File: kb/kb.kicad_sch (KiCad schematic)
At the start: 90 parts, among them SW1 SW_Push, SW10 SW_Push, SW11 SW_Push, SW12 SW_Push, SW13 SW_Push, SW14 SW_Push, SW15 SW_Push, SW16 SW_Push, SW17 SW_Push, SW18 SW_Push, SW19 SW_Push, SW2 SW_Push, SW20 SW_Push, SW21 SW_Push, SW22 SW_Push, SW23 SW_Push, SW24 SW_Push, SW25 SW_Push, SW26 SW_Push, SW27 SW_Push, SW28 SW_Push, SW29 SW_Push, SW3 SW_Push, SW30 SW_Push, SW31 SW_Push, SW32 SW_Push, SW33 SW_Push, SW34 SW_Push, SW35 SW_Push, SW36 SW_Push, SW37 SW_Push, SW38 SW_Push, SW39 SW_Push, SW4 SW_Push, SW40 SW_Push, SW41 SW_Push, SW42 SW_Push, SW43 SW_Push, SW44 SW_Push, SW45 SW_Push, SW5 SW_Push, SW6 SW_Push, SW7 SW_Push, SW8 SW_Push, SW9 SW_Push

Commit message: Updated Schematic
Updated Schematic
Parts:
- added D46: D, Diode_SMD:D_0201_0603Metric, symbol Device:D
- added SW24: SW_Push, MX_Solderable:MX-Solderable-1.5U, symbol Switch:SW_Push
- SW1: footprint MX_Solderable:MX-Solderable-1U -> MX_Solderable:MX-Solderable-1.5U
- SW12, SW13: footprint MX_Solderable:MX-Solderable-1U -> MX_Solderable:MX-Solderable-1.75U
- SW25: renamed from SW24; footprint MX_Solderable:MX-Solderable-1U -> MX_Solderable:MX-Solderable-2.25U
- SW37: renamed from SW36; footprint MX_Solderable:MX-Solderable-1U -> MX_Solderable:MX-Solderable-1.25U
- SW39: renamed from SW38; footprint MX_Solderable:MX-Solderable-1U -> MX_Solderable:MX-Solderable-1.25U
- SW40: renamed from SW39; footprint MX_Solderable:MX-Solderable-1U -> MX_Solderable:MX-Solderable-2.25U
- SW42: renamed from SW41; footprint MX_Solderable:MX-Solderable-1U -> MX_Solderable:MX-Solderable-2.25U
- SW43: renamed from SW42; footprint MX_Solderable:MX-Solderable-1U -> MX_Solderable:MX-Solderable-1.25U
- renumbered SW25 to SW26, SW26 to SW27, SW27 to SW28, SW28 to SW29, SW29 to SW30, SW30 to SW31, SW31 to SW32, SW32 to SW33, SW33 to SW34, SW34 to SW35, SW35 to SW36, SW37 to SW38, SW40 to SW41, SW43 to SW44, SW44 to SW45, SW45 to SW46
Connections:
- net COL11: now also SW24.1
- net ROW1: now also D46.1 (K)
- new net: D46.2 (A), SW24.2

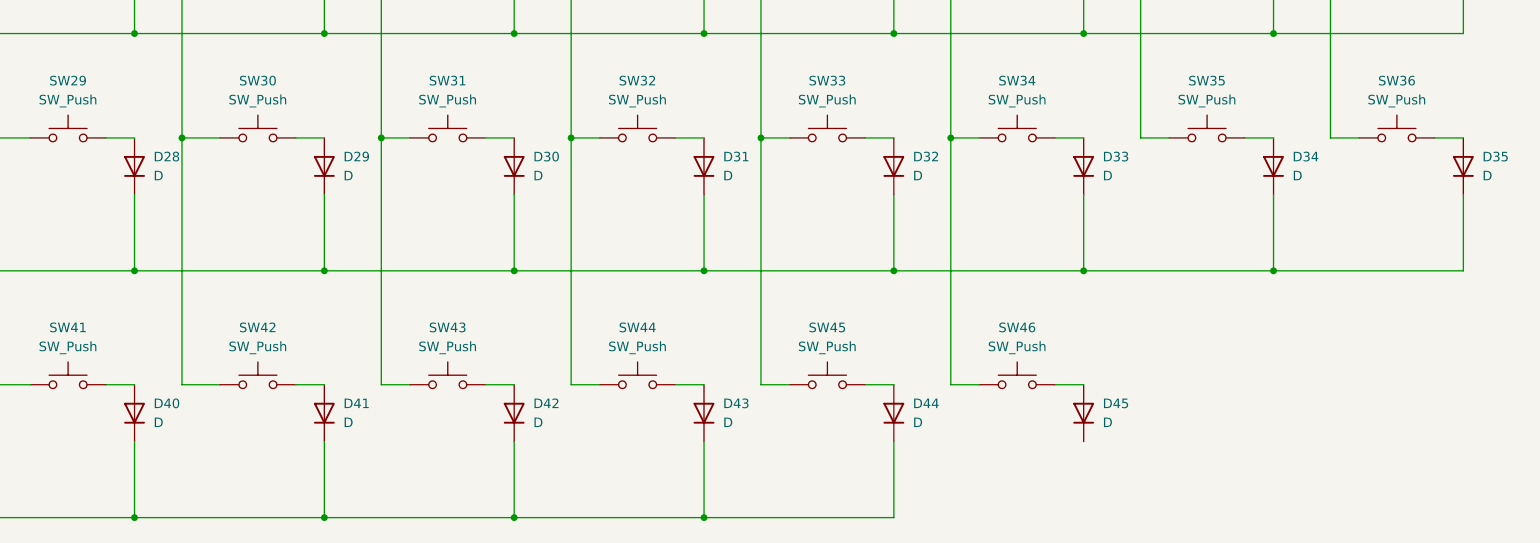
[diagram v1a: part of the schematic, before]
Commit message: Improved routing
Edited schematic column layout,
Manually routed necessary keys on pcb
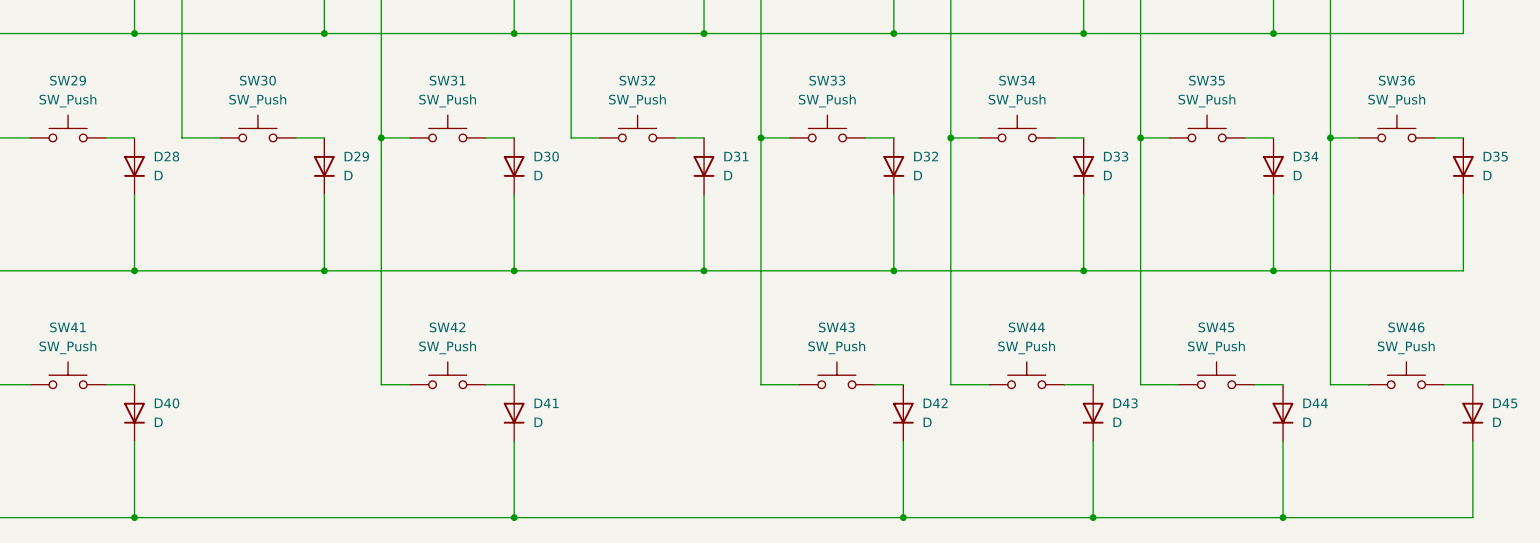
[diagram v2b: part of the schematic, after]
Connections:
- net COL10: now also SW45.1
- net COL11: now also SW46.1
- net COL5: no longer SW42.1
- net COL6: now also SW42.1; no longer SW43.1
- net COL7: no longer SW44.1
- net COL8: now also SW43.1; no longer SW45.1
- net COL9: now also SW44.1; no longer SW46.1
- net ROW3: now also D45.1 (K)
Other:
- moved on the sheet: D41, D42, D43, D44, D45, SW42, SW43, SW44, SW45, SW46

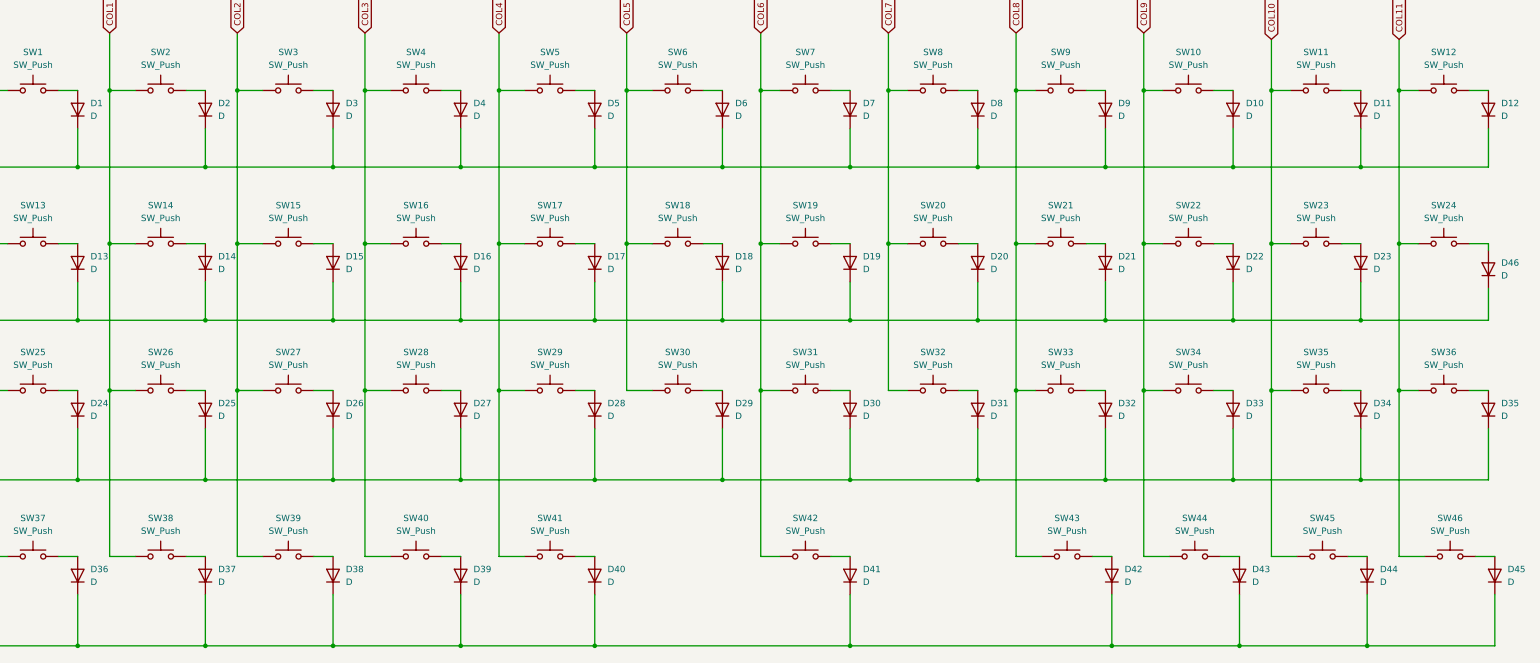
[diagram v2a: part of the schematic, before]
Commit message: 1.5u enter, fixed schematic
Fixed schematic & pcb for 1.5u enter layout
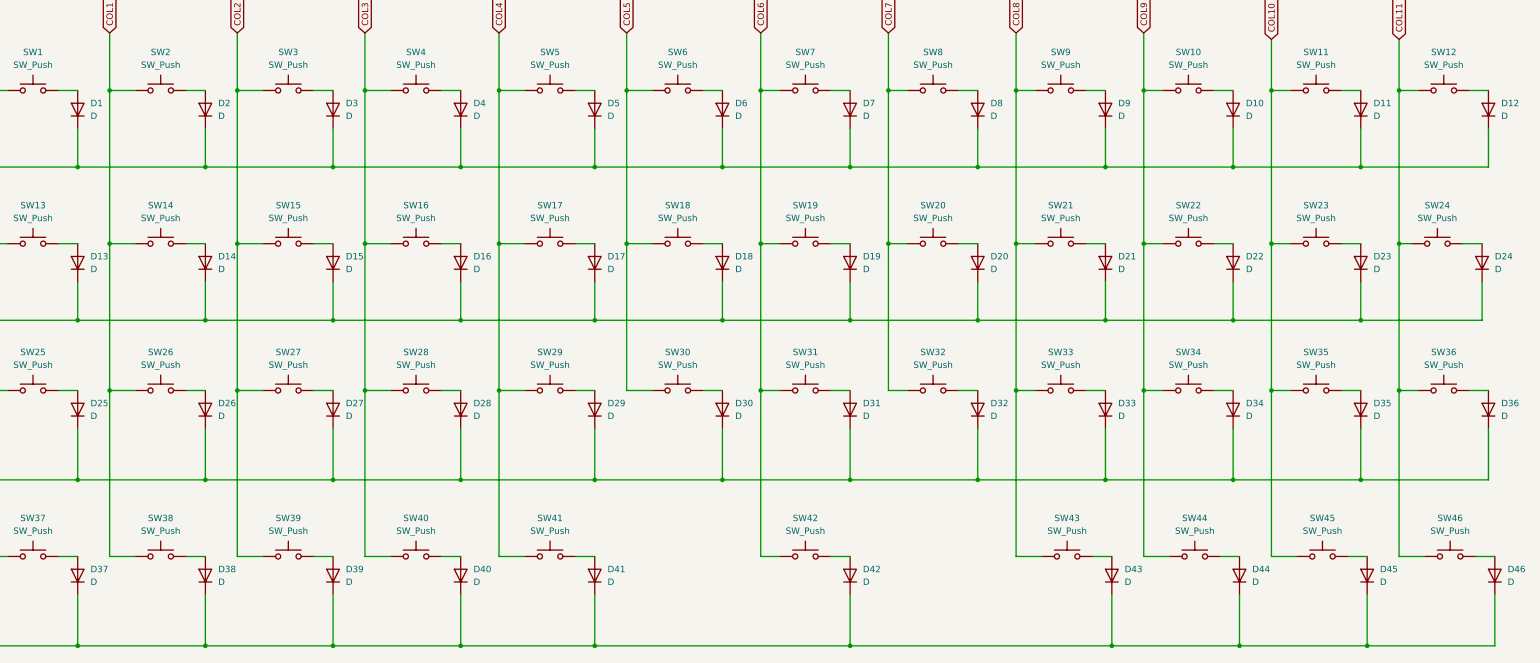
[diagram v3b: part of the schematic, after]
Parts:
- removed D46: D, Diode_SMD:D_0201_0603Metric, symbol Device:D
- added D24: D, Diode_SMD:D_0201_0603Metric, symbol Device:D
- renumbered D24 to D25, D25 to D26, D26 to D27, D27 to D28, D28 to D29, D29 to D30, D30 to D31, D31 to D32, D32 to D33, D33 to D34, D34 to D35, D35 to D36, D36 to D37, D37 to D38, D38 to D39, D39 to D40, D40 to D41, D41 to D42, D42 to D43, D43 to D44, D44 to D45, D45 to D46
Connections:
- net ROW1: now also D24.1 (K)
- net at SW24.2: now also D24.2 (A)

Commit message: STM32 + Unified Daughterboard Implementation
Switched to run off STM32 and S1.1 Unified Daughterboard.
Wired rows and cols
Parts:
- added C10, C12, C9: 1uF, Capacitor_SMD:C_0805_2012Metric, symbol Device:C_Small
- added C11: 10nF, Capacitor_SMD:C_0805_2012Metric, symbol Device:C_Small
- added C13, C8: 100nF, Capacitor_SMD:C_0805_2012Metric, symbol Device:C_Small
- added C14, C4: 4.7uF, Capacitor_SMD:C_0805_2012Metric, symbol Device:C_Small
- added C2, C3: 0.1uF, Capacitor_SMD:C_0805_2012Metric, symbol Device:C_Small
- added C5: .1uF, Capacitor_SMD:C_0805_2012Metric, symbol Device:C_Small
- added J1: Conn_01x04_MountingPin, Connector_Molex:Molex_Pico-EZmate_78171-0004_1x04-1MP_P1.20mm_Vertical, symbol Connector_Generic_MountingPin:Conn_01x04_MountingPin
- added R5: 10k, Resistor_SMD:R_0805_2012Metric, symbol Device:R_Small
- added SW48: SW_Push, Button_Switch_SMD:SW_SPST_SKQG_WithStem, symbol Switch:SW_Push
- added U1: USBLC6-2SC6, Package_TO_SOT_SMD:SOT-23-6, symbol Power_Protection:USBLC6-2SC6
- added U2: STM32G474CETx, Package_QFP:LQFP-48_7x7mm_P0.5mm, symbol MCU_ST_STM32G4:STM32G474CETx
- added U4: XC6206PxxxMR, Package_TO_SOT_SMD:SOT-23-3, symbol Regulator_Linear:XC6206PxxxMR
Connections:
- net COL1: now also U2.11 (PA3)
- net COL10: now also U2.28 (PB14)
- net COL11: now also U2.27 (PB13)
- net COL2: now also U2.10 (PA2)
- net COL3: now also U2.9 (PA1)
- net COL4: now also U2.32 (PA10)
- net COL5: now also U2.34 (PA12)
- net COL6: now also U2.31 (PA9)
- net COL7: now also U2.33 (PA11)
- net COL8: now also U2.30 (PA8)
- net COL9: now also U2.29 (PB15)
- net ROW0: now also U2.42 (PB5)
- net ROW1: now also U2.43 (PB6)
- net ROW2: now also U2.44 (PB7)
- net ROW3: now also U2.16 (PB0)
- net Col0 renamed COL0
- net COL0: now also U2.12 (PA4)
- new net: C8.2, U2.20 (VREF+)
- new net +3V3: C10.2, C11.1, C12.1, C13.1, C14.1, C2.1, C3.1, C4.1, C5.1, SW48.1, U2.1 (VBAT), U2.21 (VDDA), U2.24 (VDD), U2.36 (VDD), U2.48 (VDD), U4.2 (VO)
- new net +5V: C9.2, J1.1 (Pin_1), U1.5 (VBUS), U4.3 (VI)
- new net BOOT: R5.1, SW48.2, U2.7 (PG10)
- new net D+: J1.3 (Pin_3), U1.1 (I/O1), U1.6 (I/O1), U2.26 (PB12)
- new net D-: J1.2 (Pin_2), U1.3 (I/O2), U1.4 (I/O2), U2.25 (PB11)
- new net GND: C10.1, C11.2, C12.2, C13.2, C14.2, C2.2, C3.2, C4.2, C5.2, C8.1, C9.1, J1.4 (Pin_4), J1.MP (MountPin), R5.2, U1.2 (GND), U2.19 (VSSA), U2.23 (VSS), U2.35 (VSS), U2.47 (VSS), U4.1 (GND)
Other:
- note added: "Switch Matrix"
- moved on the sheet: D1, D10, D11, D12, D13, D14, D15, D16, D17, D18, D19, D2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

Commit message: Fixed Board Side
Fixed Side of board
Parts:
- C13: value 100nF -> 0.1uF
- D1, D10, D11, D12, D13, D14, D15, D16, D17, D18, D19, D2, D20, D21, D22, D23, D24, D25, D26, D27, D28, D29, D3, D30, D31, D32, D33, D34, D35, D36, D37, D38, D39, D4, D40, D41, D42, D43, D44, D45, D46, D5, D6, D7, D8, D9: footprint Diode_SMD:D_0201_0603Metric -> Diode_SMD:D_0805_2012Metric
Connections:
- net COL0: now also U2.37 (PA13); no longer U2.12 (PA4)
- net COL1: now also U2.38 (PA14); no longer U2.11 (PA3)
- net COL10: now also U2.11 (PA3); no longer U2.28 (PB14)
- net COL11: now also U2.12 (PA4); no longer U2.27 (PB13)
- net COL2: now also U2.39 (PA15); no longer U2.10 (PA2)
- net COL3: now also U2.40 (PB3); no longer U2.9 (PA1)
- net COL4: now also U2.41 (PB4); no longer U2.32 (PA10)
- net COL5: now also U2.42 (PB5); no longer U2.34 (PA12)
- net COL6: now also U2.43 (PB6); no longer U2.31 (PA9)
- net COL7: now also U2.8 (PA0); no longer U2.33 (PA11)
- net COL8: now also U2.9 (PA1); no longer U2.30 (PA8)
- net COL9: now also U2.10 (PA2); no longer U2.29 (PB15)
- net ROW0: now also U2.44 (PB7); no longer U2.42 (PB5)
- net ROW1: now also U2.45 (PB8); no longer U2.43 (PB6)
- net ROW2: now also U2.46 (PB9); no longer U2.44 (PB7)
- net ROW3: now also U2.13 (PA5); no longer U2.16 (PB0)

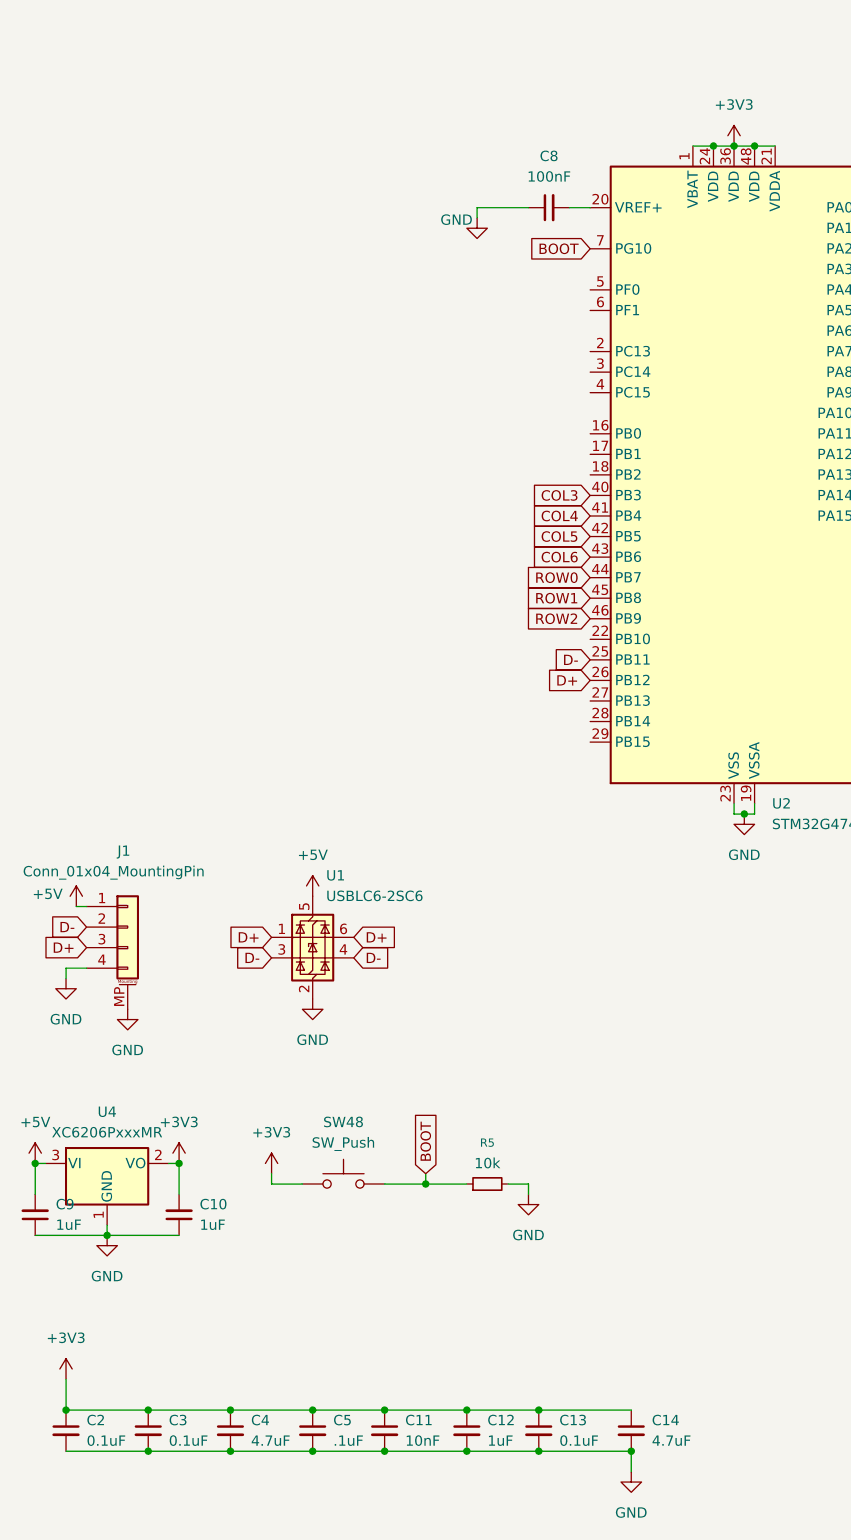
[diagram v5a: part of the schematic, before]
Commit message: Fixed Decoupling
Fix decoupling cap placement + amounts, added ground layer, thickened vdd traces, completed routing
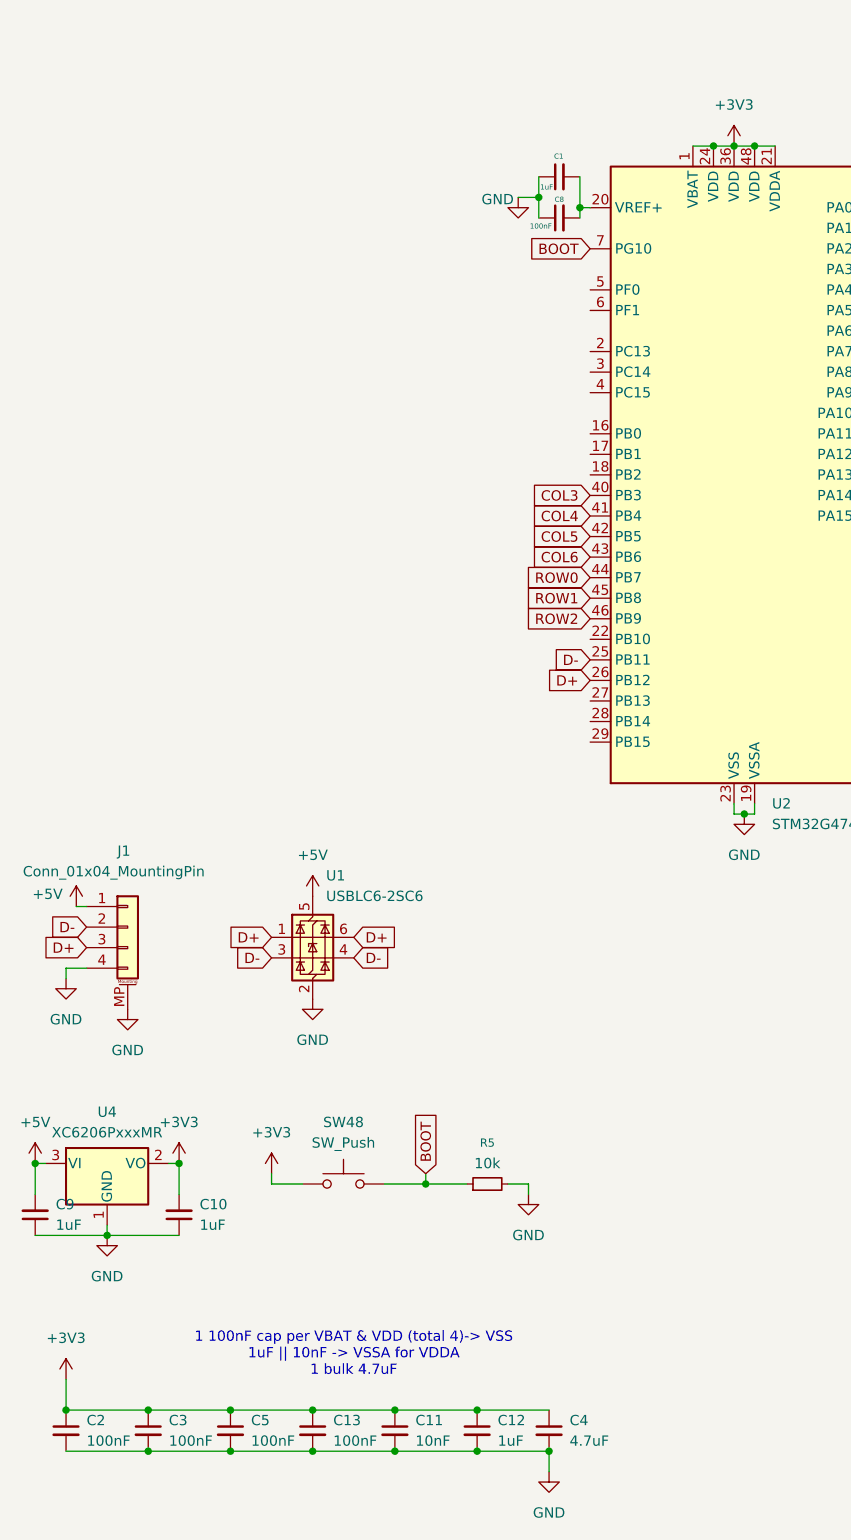
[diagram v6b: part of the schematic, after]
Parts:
- removed C14: 4.7uF, Capacitor_SMD:C_0805_2012Metric, symbol Device:C_Small
- added C1: 1uF, Capacitor_SMD:C_0805_2012Metric, symbol Device:C_Small
- C13, C2, C3: value 0.1uF -> 100nF
- C5: value .1uF -> 100nF
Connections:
- net GND: now also C1.1
- net at C8.2, U2.20 (VREF+): now also C1.2
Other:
- note added: "1 100nF cap per VBAT & VDD (total 4)-> VSS 1uF || 10nF -> VSSA for VDDA 1 bulk 4.7uF"
- moved on the sheet: C11, C12, C13, C4, C5, C8
